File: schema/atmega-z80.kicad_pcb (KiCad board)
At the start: 2 copper layers, 142.2 x 115.6 mm, 75 parts, among them J1 USB Connector, J2 Programmer ISP 10, J3 SPI Connector, J4 I2C Connector, Q1 PNP_2N4403, Q2 PNP_2N4403, Q3 NPN_2N4401, Q4 PNP_2N4403, U1 Z84C0010PEG, U2 ATmega324A-PU, U3 AS6C4008-55PCN, U4 SN74HC373N, U5 SN74HC257, U6 SN74HC257, U7 SN74HC00, U8 MCP2221AxP, Y1 20MHz

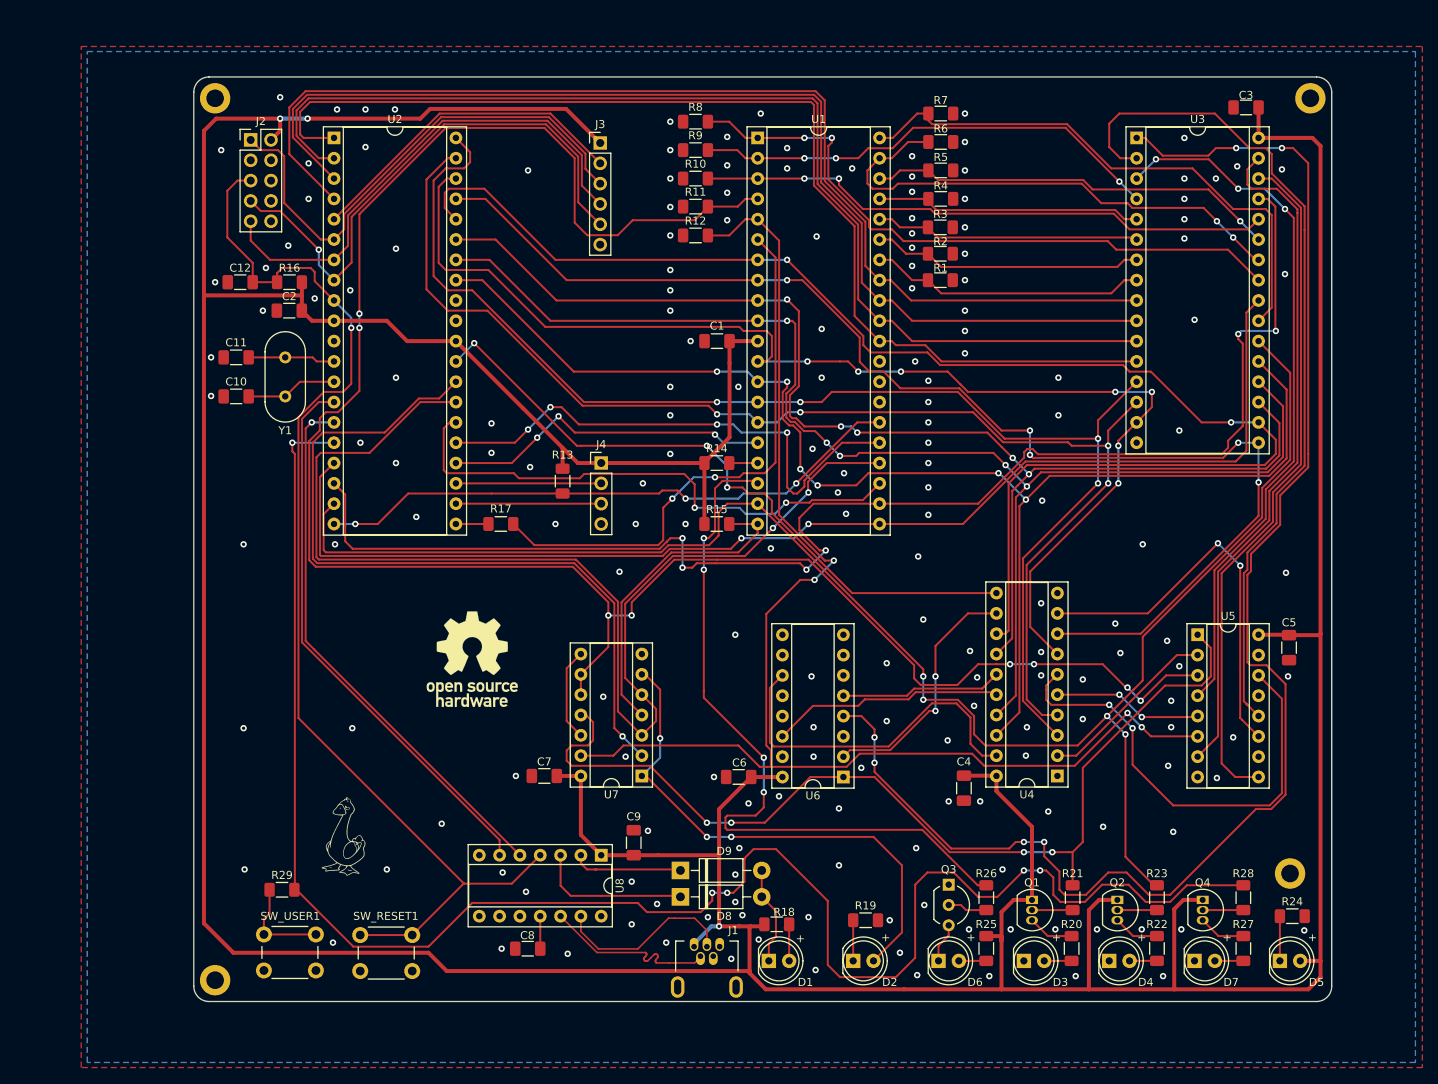
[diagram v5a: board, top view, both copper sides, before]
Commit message: Moved USB-mini connector to the left to prevent crossing of VDD and USB data lines.
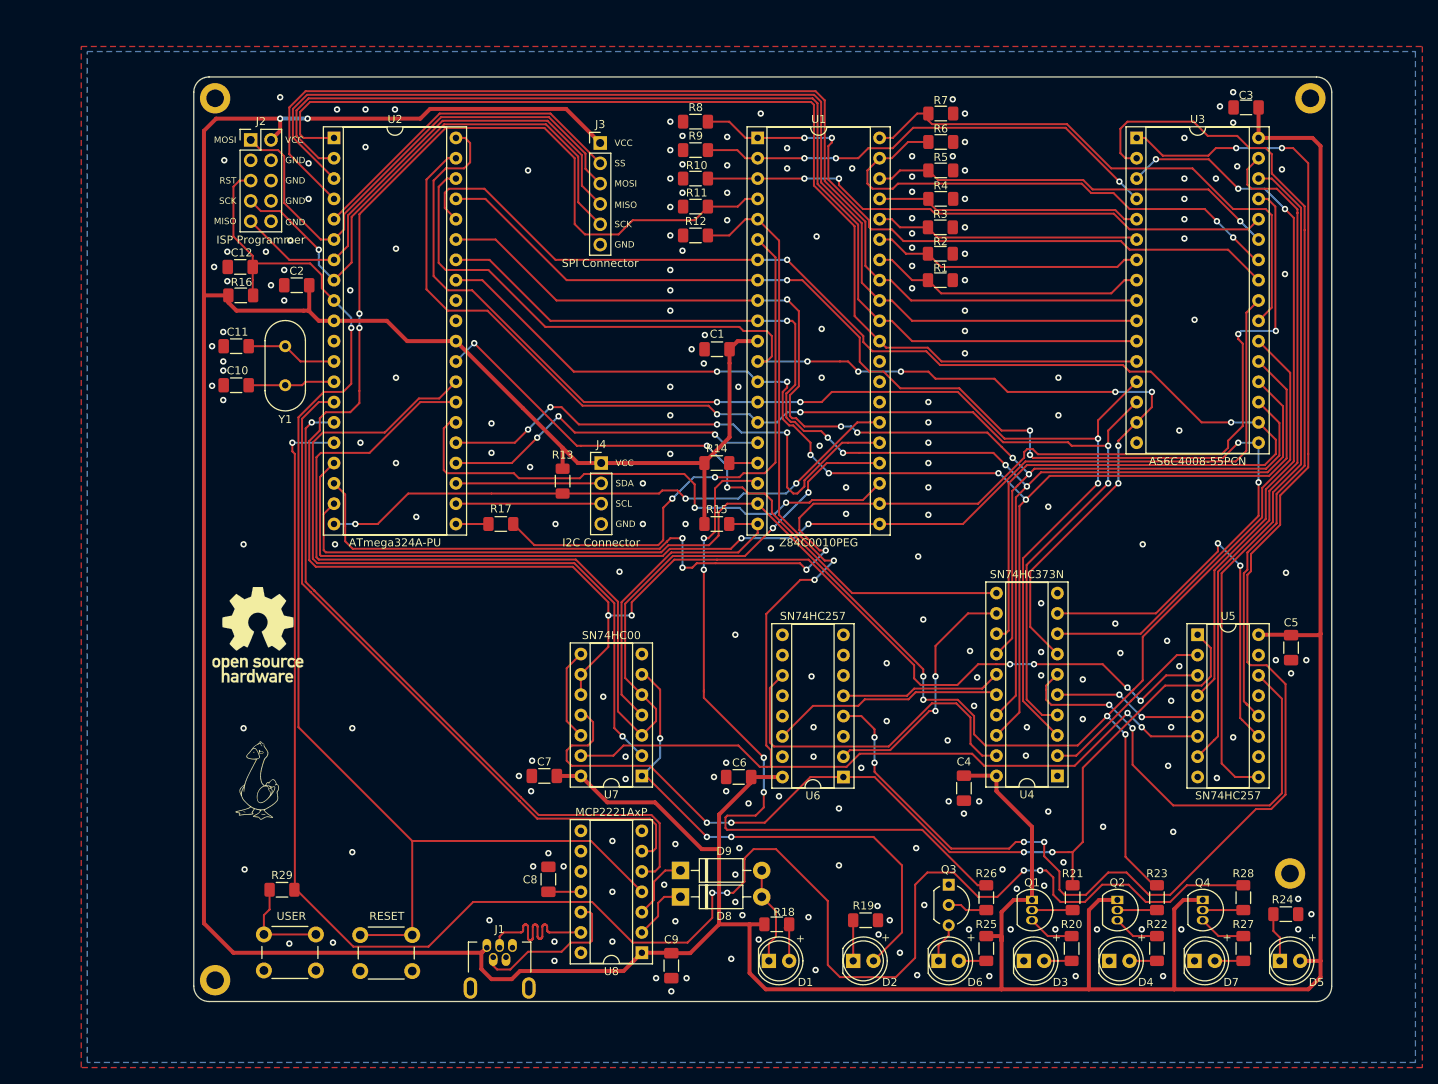
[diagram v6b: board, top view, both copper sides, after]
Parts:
- J2: value Programmer ISP 10 -> ISP Programmer
- SW_RESET1: value SW_Push -> RESET
- SW_USER1: value SW_Push -> USER
- moved REF** 27.0 mm to (79.8, 106.6)
- moved J1 25.9 mm to (110.0, 148.7)
- moved C9 16.1 mm to (131.4, 147.9), turned to 270 degrees
- moved U8 13.2 mm to (127.8, 146.3), turned to 180 degrees
- moved G*** 12.9 mm to (79.9, 124.8)
- moved C8 9.05 mm to (116.1, 137.1), turned to 90 degrees
- moved R16 6.32 mm to (77.6, 64.1), turned to 0 degrees
- moved C2 3.31 mm to (84.6, 62.9)
- moved C12 1.91 mm to (77.6, 60.6)
- moved C10 1.40 mm to (77.1, 75.4)
- moved C11 1.40 mm to (77.1, 70.5)
- moved Y1 1.40 mm to (83.2, 70.5)
- moved C1 1.02 mm to (137.2, 70.9)
- moved R24 0.85 mm to (208.3, 141.5)
- moved C5 0.25 mm to (208.9, 108.2)
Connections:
- U8 pad 2: Net-(D9-Pad1) -> Net-(D8-Pad1)
- U8 pad 3: Net-(D8-Pad1) -> Net-(D9-Pad1)
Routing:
- net /ATMEGA_TX_AND_USB_RX: track 68.3 -> 87.7 mm
- net /ATMEGA_RX_AND_USB_TX: track 69.6 -> 87.0 mm
- net /#SYS_RESET: track 142.9 -> 158.0 mm
- net Net-(D8-Pad1): track 19.3 -> 7.63 mm
- net +5V: track 665.1 -> 658.7 mm, vias 3 -> 2
- net Net-(D9-Pad1): track 13.9 -> 8.32 mm
- net #USER_LED: track 221.4 -> 225.9 mm
- net Net-(U3-Pad2): track 106.0 -> 102.4 mm
- net /D7: track 169.1 -> 166.0 mm
- net /USB_D+: track 22.8 -> 19.8 mm
- net /USB_D-: track 22.8 -> 19.9 mm
- net SPI_MISO: track 63.1 -> 61.7 mm
- net Net-(C11-Pad2): track 10.9 -> 11.8 mm
- net /A14: track 254.7 -> 255.6 mm
- net /D0: track 165.6 -> 166.3 mm
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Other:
- board text added: "GND"
- board text added: "MISO"
- board text added: "MOSI"
- board text added: "RST"
- board text added: "SCK"
- board text added: "SCL"
- board text added: "SDA"
- board text added: "SS"
- board text added: "VCC"

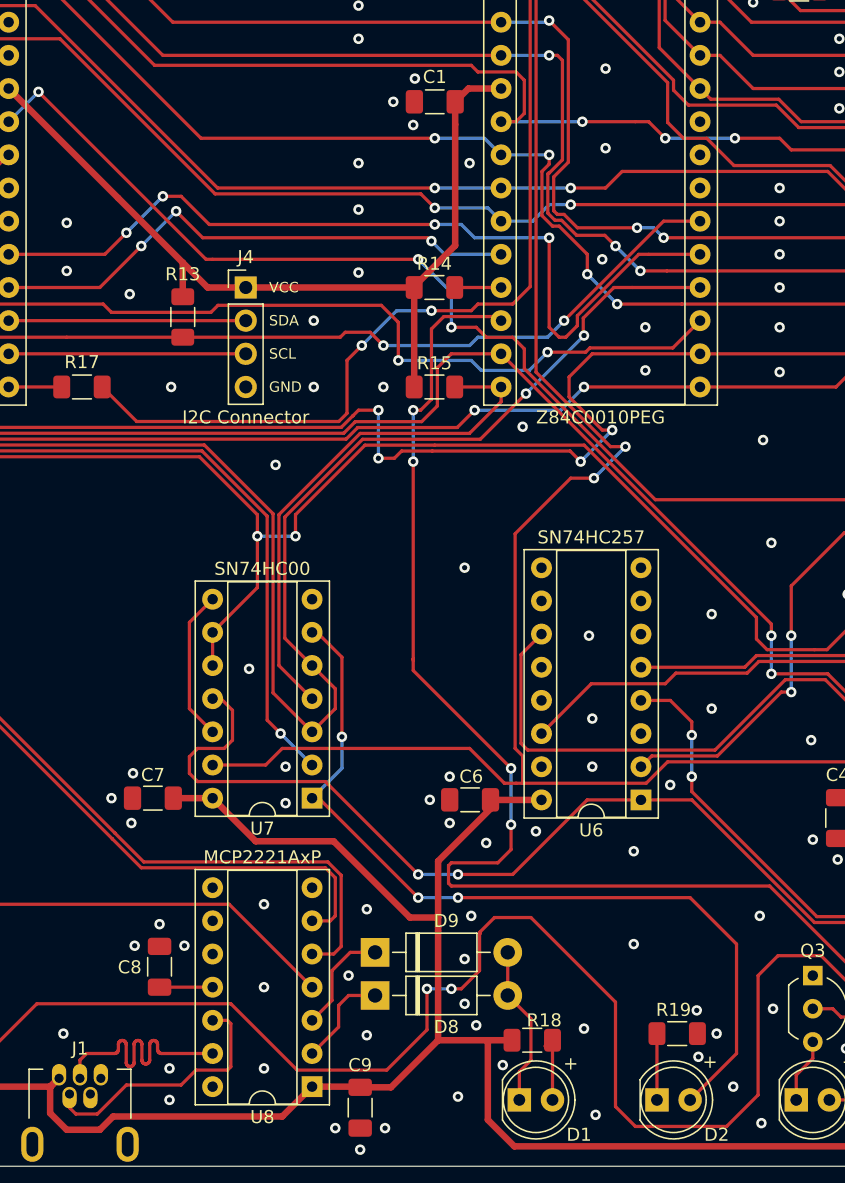
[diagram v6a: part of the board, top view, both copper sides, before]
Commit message: Added some more ground vias to PCB
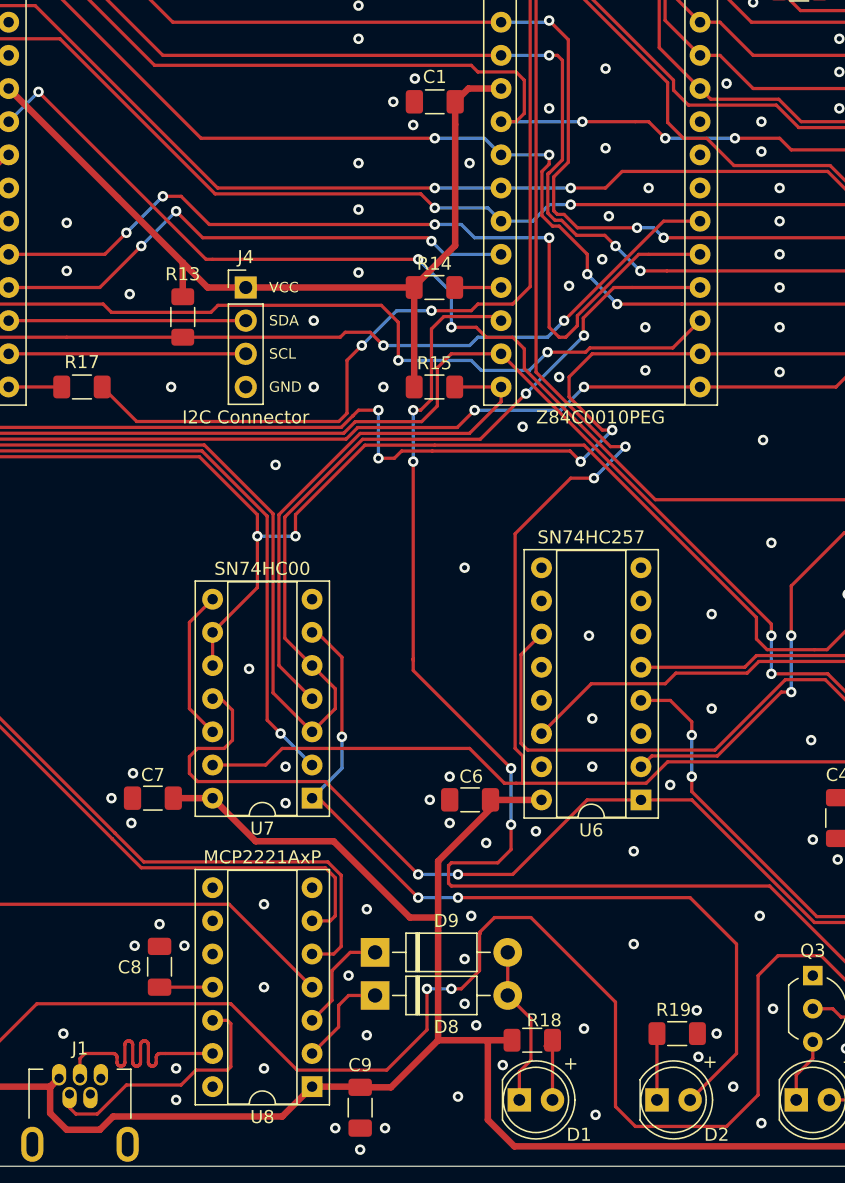
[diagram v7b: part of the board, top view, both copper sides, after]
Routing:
- net GND: vias 221 -> 229
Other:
- rule via_min_drill: 0.3 -> 0.2
- rule via_min_size: 0.4 -> 0.45
